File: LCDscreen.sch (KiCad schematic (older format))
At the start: 12 parts

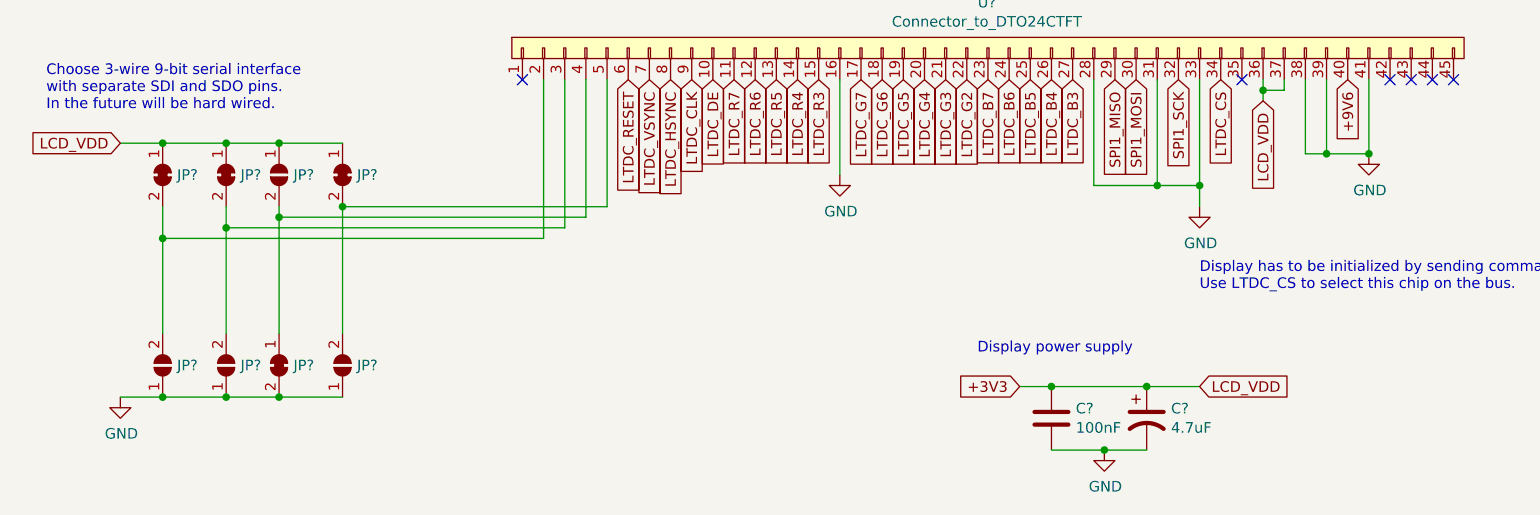
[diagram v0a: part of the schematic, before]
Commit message: First proposed pin layout of SODIMM connector
Will need to add GPIO / ADC pins as needed, but let's wait to see if we don't
need to use more pins.

Double-checked and fixed CODEC and MCU's power supply.
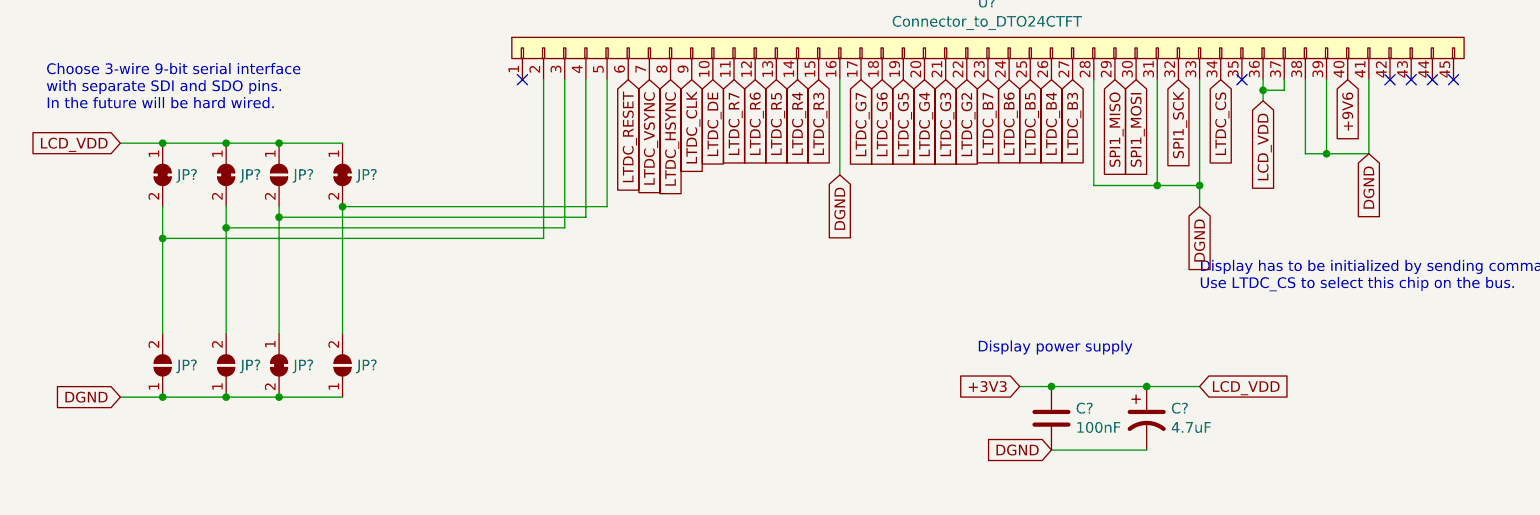
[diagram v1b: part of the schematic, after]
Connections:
- net GND renamed DGND
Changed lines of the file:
@@
 $Descr A4 11693 8268
 encoding utf-8
-Sheet 9 12
+Sheet 9 13
 Title ""
 Date ""
@@
 Text GLabel 9350 3350 3    50   Input ~ 0
 +9V6
-$Comp
-L power:GND #PWR?
-U 1 1 5CFFF94F
-P 9450 3700
-F 0 "#PWR?" H 9450 3450 50  0001 C CNN
-F 1 "GND" H 9455 3527 50  0000 C CNN
-F 2 "" H 9450 3700 50  0001 C CNN
-F 3 "" H 9450 3700 50  0001 C CNN
-	1    9450 3700
-	1    0    0    -1
-$EndComp
 Wire Wire Line
 	9450 3350 9450 3700
@@
 Wire Wire Line
 	9250 3700 9450 3700
-Connection ~ 9450 3700
 Wire Wire Line
 	9150 3350 9150 3700
@@
 Wire Wire Line
 	7800 4800 7950 4800
-$Comp
-L power:GND #PWR?
-U 1 1 5CFFFAE0
-P 8200 5100
-AR Path="/5CFEB435/5CFFFAE0" Ref="#PWR?"  Part="1"
-AR Path="/5CFEBF88/5CFFFAE0" Ref="#PWR?"  Part="1"
-F 0 "#PWR?" H 8200 4850 50  0001 C CNN
-F 1 "GND" H 8205 4927 50  0000 C CNN
-F 2 "" H 8200 5100 50  0001 C CNN
-F 3 "" H 8200 5100 50  0001 C CNN
-	1    8200 5100
-	1    0    0    -1
-$EndComp
 $Comp
 L Device:C C?
@@
 Wire Wire Line
 	8400 4800 8650 4800
-Wire Wire Line
-	8200 5100 8400 5100
-Connection ~ 8200 5100
 Connection ~ 7950 4800
 Wire Wire Line
 	7950 4800 8400 4800
-Wire Wire Line
-	7950 5100 8200 5100
 Text GLabel 3550 3650 0    50   Input ~ 0
 LCD_VDD
@@
 	3750 4850 4050 4850
 Connection ~ 4050 4850
-$Comp
-L power:GND #PWR?
-U 1 1 5D002170
-P 3550 4850
-F 0 "#PWR?" H 3550 4600 50  0001 C CNN
-F 1 "GND" H 3555 4677 50  0000 C CNN
-F 2 "" H 3550 4850 50  0001 C CNN
-F 3 "" H 3550 4850 50  0001 C CNN
-	1    3550 4850
-	1    0    0    -1
-$EndComp
 Wire Wire Line
 	3750 4100 3750 4550
@@
 Text GLabel 6350 3350 3    50   Input ~ 0
 LTDC_DE
-$Comp
-L power:GND #PWR?
-U 1 1 5CFFF432
-P 6950 3800
-F 0 "#PWR?" H 6950 3550 50  0001 C CNN
-F 1 "GND" H 6955 3627 50  0000 C CNN
-F 2 "" H 6950 3800 50  0001 C CNN
-F 3 "" H 6950 3800 50  0001 C CNN
-	1    6950 3800
-	1    0    0    -1
-$EndComp
 Wire Wire Line
 	6950 3800 6950 3350
@@
 Text Notes 8650 4350 0    50   ~ 0
 Display has to be initialized by sending commands via SPI.\nUse LTDC_CS to select this chip on the bus.
-$Comp
-L power:GND #PWR?
-U 1 1 5D007F92
-P 8650 3950
-F 0 "#PWR?" H 8650 3700 50  0001 C CNN
-F 1 "GND" H 8655 3777 50  0000 C CNN
-F 2 "" H 8650 3950 50  0001 C CNN
-F 3 "" H 8650 3950 50  0001 C CNN
-	1    8650 3950
-	1    0    0    -1
-$EndComp
 Text GLabel 8250 3350 3    50   Input ~ 0
 SPI1_MISO
@@
 Text Notes 7600 4650 0    50   ~ 0
 Display power supply
+Text GLabel 9450 3700 3    50   Input ~ 0
+DGND
+Wire Wire Line
+	7950 5100 8400 5100
+Text GLabel 7950 5100 0    50   Input ~ 0
+DGND
+Text GLabel 3550 4850 0    50   Input ~ 0
+DGND
+Text GLabel 6950 3800 3    50   Input ~ 0
+DGND
+Text GLabel 8650 3950 3    50   Input ~ 0
+DGND
 $EndSCHEMATC
